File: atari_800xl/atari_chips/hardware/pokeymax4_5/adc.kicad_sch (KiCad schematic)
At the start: 5 parts

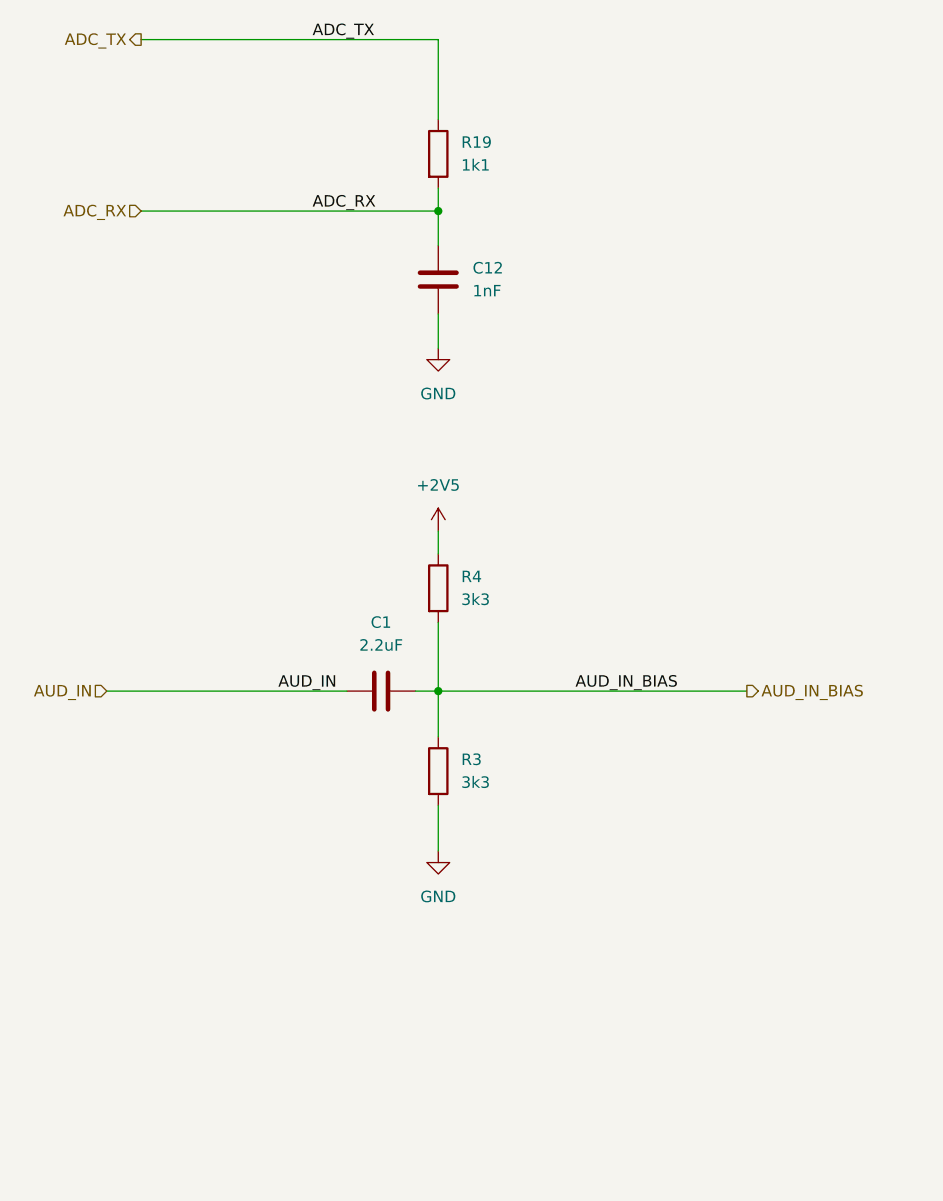
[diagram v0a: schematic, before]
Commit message: After testing 4b first run, there are a few issues. Updated to 4b2 with: Corrected L/R output. ADC bias improvement. ADC preamp out/in- corrected. Moved silkscreen name!
git-svn-id: svn+ssh://192.168.0.3/home/svnfpga/repo/trunk@1476 d6161ac3-aae1-4d52-9b05-ea9ac36b53d3
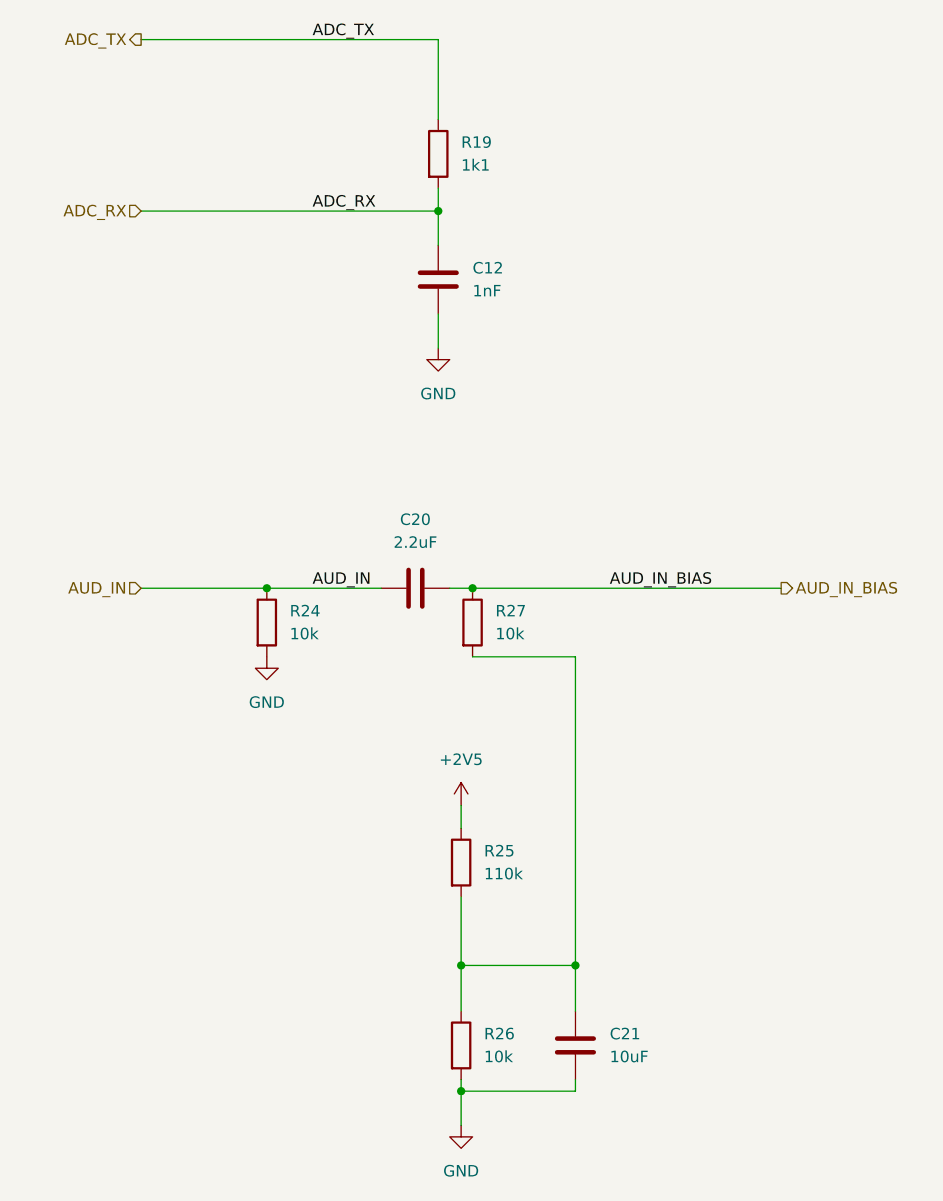
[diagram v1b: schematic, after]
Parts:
- removed C1: 2.2uF, Capacitor_SMD:C_0603_1608Metric, symbol Device:C
- removed R3, R4: 3k3, Resistor_SMD:R_0603_1608Metric, symbol Device:R
- added C20: 2.2uF, Capacitor_SMD:C_0603_1608Metric, symbol Device:C
- added C21: 10uF, Capacitor_SMD:C_0603_1608Metric, symbol Device:C
- added R24, R26, R27: 10k, Resistor_SMD:R_0603_1608Metric, symbol Device:R
- added R25: 110k, Resistor_SMD:R_0603_1608Metric, symbol Device:R
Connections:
- net +2V5: now also R25.1
- net AUD_IN: now also C20.1, R24.1
- net AUD_IN_BIAS: now also C20.2, R27.1
- net GND: now also C21.1, R24.2, R26.2
- new net: C21.2, R25.2, R26.1, R27.2

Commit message: Pokeymax v4_53 as produced
git-svn-id: svn+ssh://192.168.0.3/home/svnfpga/repo/trunk@1512 d6161ac3-aae1-4d52-9b05-ea9ac36b53d3
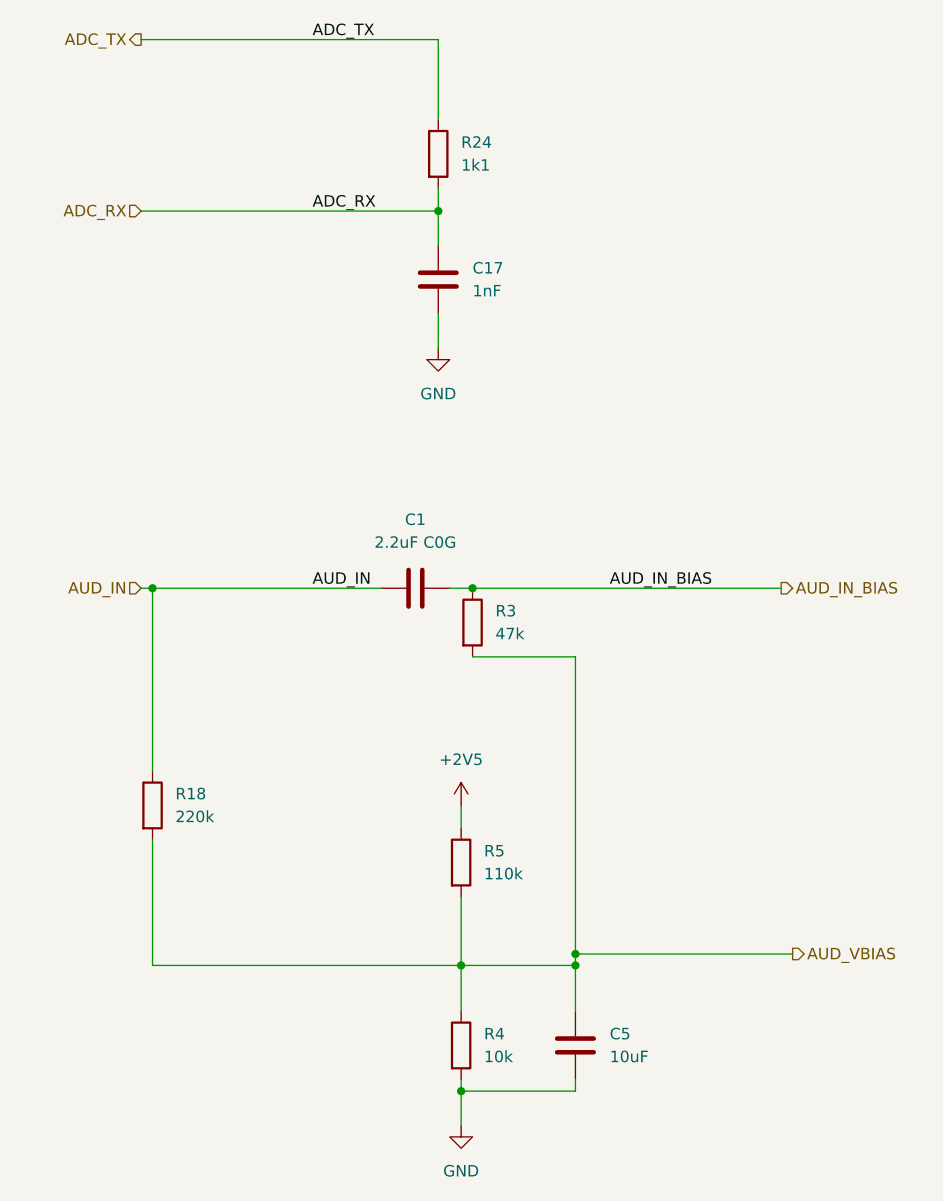
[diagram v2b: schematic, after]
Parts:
- removed R24: 10k, Resistor_SMD:R_0603_1608Metric, symbol Device:R
- added R18: 220k, Resistor_SMD:R_0603_1608Metric, symbol Device:R
- C1: renamed from C20; value 2.2uF -> 2.2uF C0G
- C17: renamed from C12; footprint Capacitor_SMD:C_0603_1608Metric -> Capacitor_SMD:C_0402_1005Metric
- R24: renamed from R19; footprint Resistor_SMD:R_0603_1608Metric -> Resistor_SMD:R_0402_1005Metric
- R3: renamed from R27; value 10k -> 47k
- renumbered C21 to C5, R26 to R4, R25 to R5
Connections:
- net AUD_IN: now also R18.1
- net AUD_VBIAS: now reaches C5.2, R3.2, R4.1, R5.2
- net AUD_VBIAS: now also R18.2
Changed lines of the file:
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@@
 	(paper "A4")
+	(junction
+		(at 80.01 133.35)
+		(diameter 0)
+		(color 0 0 0 0)
+	)
+	(junction
+		(at 33.02 92.71)
+		(diameter 0)
+		(color 0 0 0 0)
+	)
 	(junction
 		(at 80.01 134.62)
@@
 	)
 	(junction
-		(at 45.72 92.71)
-		(diameter 0)
-		(color 0 0 0 0)
-	)
-	(junction
 		(at 68.58 92.71)
 		(diameter 0)
@@
 	(wire
 		(pts
+			(xy 33.02 120.65) (xy 33.02 134.62)
+		)
+		(stroke
+			(width 0)
+			(type default)
+		)
+	)
+	(wire
+		(pts
 			(xy 80.01 100.33) (xy 68.58 100.33)
 		)
@@
 	(wire
 		(pts
-			(xy 80.01 100.33) (xy 80.01 134.62)
+			(xy 80.01 133.35) (xy 104.14 133.35)
+		)
+		(stroke
+			(width 0)
+			(type default)
+		)
+	)
+	(wire
+		(pts
+			(xy 80.01 100.33) (xy 80.01 133.35)
 		)
 		(stroke
@@
 	(wire
 		(pts
-			(xy 31.75 92.71) (xy 45.72 92.71)
+			(xy 31.75 92.71) (xy 33.02 92.71)
 		)
 		(stroke
@@
 	(wire
 		(pts
+			(xy 33.02 92.71) (xy 33.02 113.03)
+		)
+		(stroke
+			(width 0)
+			(type default)
+		)
+	)
+	(wire
+		(pts
 			(xy 64.77 62.23) (xy 64.77 66.04)
 		)
@@
 	(wire
 		(pts
+			(xy 80.01 133.35) (xy 80.01 134.62)
+		)
+		(stroke
+			(width 0)
+			(type default)
+		)
+	)
+	(wire
+		(pts
 			(xy 80.01 139.7) (xy 80.01 134.62)
 		)
@@
 	(wire
 		(pts
-			(xy 45.72 92.71) (xy 58.42 92.71)
+			(xy 33.02 134.62) (xy 67.31 134.62)
+		)
+		(stroke
+			(width 0)
+			(type default)
+		)
+	)
+	(wire
+		(pts
+			(xy 33.02 92.71) (xy 58.42 92.71)
 		)
 		(stroke
@@
 		)
 	)
+	(hierarchical_label "AUD_VBIAS"
+		(shape output)
+		(at 104.14 133.35 0)
+		(effects
+			(font
+				(size 1.27 1.27)
+			)
+			(justify left)
+		)
+	)
 	(hierarchical_label "ADC_TX"
 		(shape output)
@@
 			)
 			(justify right)
+		)
+	)
+	(symbol
+		(lib_id "Device:R")
+		(at 33.02 116.84 0)
+		(unit 1)
+		(exclude_from_sim no)
+		(in_bom yes)
+		(on_board yes)
+		(dnp no)
+		(fields_autoplaced yes)
+		(property "Reference" "R18"
+			(at 35.56 115.5699 0)
+			(effects
+				(font
+					(size 1.27 1.27)
+				)
+				(justify left)
+			)
+		)
+		(property "Value" "220k"
+			(at 35.56 118.1099 0)
+			(effects
+				(font
+					(size 1.27 1.27)
+				)
+				(justify left)
+			)
+		)
+		(property "Footprint" "Resistor_SMD:R_0603_1608Metric"
+			(at 31.242 116.84 90)
+			(effects
+				(font
+					(size 1.27 1.27)
+				)
+				(hide yes)
+			)
+		)
+		(property "Datasheet" "~"
+			(at 33.02 116.84 0)
+			(effects
+				(font
+					(size 1.27 1.27)
+				)
+				(hide yes)
+			)
+		)
+		(property "Description" "Resistor"
+			(at 33.02 116.84 0)
+			(effects
+				(font
+					(size 1.27 1.27)
+				)
+				(hide yes)
+			)
+		)
+		(pin "1"
+		)
+		(pin "2"
+		)
+		(instances
+			(project "pokeymax4_5"
+				(path "/f8f92944-710a-49a0-a698-f840e5f20e15/1dc50d40-2acd-4c26-808b-1819716fc764"
+					(reference "R18")
+					(unit 1)
+				)
+			)
 		)
 	)
@@
 		(dnp no)
 		(fields_autoplaced yes)
-		(property "Reference" "R25"
+		(property "Reference" "R5"
 			(at 69.85 121.9199 0)
 			(effects
@@
 			(project "pokeymax4_5"
 				(path "/f8f92944-710a-49a0-a698-f840e5f20e15/1dc50d40-2acd-4c26-808b-1819716fc764"
-					(reference "R25")
-					(unit 1)
-				)
-			)
-		)
-	)
-	(symbol
-		(lib_id "Device:R")
-		(at 45.72 96.52 0)
-		(unit 1)
-		(exclude_from_sim no)
-		(in_bom yes)
-		(on_board yes)
-		(dnp no)
-		(fields_autoplaced yes)
-		(property "Reference" "R24"
-			(at 48.26 95.2499 0)
-			(effects
-				(font
-					(size 1.27 1.27)
-				)
-				(justify left)
-			)
-		)
-		(property "Value" "10k"
-			(at 48.26 97.7899 0)
-			(effects
-				(font
-					(size 1.27 1.27)
-				)
-				(justify left)
-			)
-		)
-		(property "Footprint" "Resistor_SMD:R_0603_1608Metric"
-			(at 43.942 96.52 90)
-			(effects
-				(font
-					(size 1.27 1.27)
-				)
-				(hide yes)
-			)
-		)
-		(property "Datasheet" "~"
-			(at 45.72 96.52 0)
-			(effects
-				(font
-					(size 1.27 1.27)
-				)
-				(hide yes)
-			)
-		)
-		(property "Description" "Resistor"
-			(at 45.72 96.52 0)
-			(effects
-				(font
-					(size 1.27 1.27)
-				)
-				(hide yes)
-			)
-		)
-		(pin "1"
-		)
-		(pin "2"
-		)
-		(instances
-			(project "pokeymax4_5"
-				(path "/f8f92944-710a-49a0-a698-f840e5f20e15/1dc50d40-2acd-4c26-808b-1819716fc764"
-					(reference "R24")
+					(reference "R5")
 					(unit 1)
 				)
@@
 		(dnp no)
 		(fields_autoplaced yes)
-		(property "Reference" "R27"
+		(property "Reference" "R3"
 			(at 71.12 95.2499 0)
 			(effects
@@
 			)
 		)
-		(property "Value" "10k"
+		(property "Value" "47k"
 			(at 71.12 97.7899 0)
 			(effects
@@
 			(project "pokeymax4_5"
 				(path "/f8f92944-710a-49a0-a698-f840e5f20e15/1dc50d40-2acd-4c26-808b-1819716fc764"
-					(reference "R27")
+					(reference "R3")
 					(unit 1)
 				)
@@
 		(dnp no)
 		(fields_autoplaced yes)
-		(property "Reference" "C20"
+		(property "Reference" "C1"
 			(at 62.23 85.09 90)
 			(effects
@@
 			)
 		)
-		(property "Value" "2.2uF"
+		(property "Value" "2.2uF C0G"
 			(at 62.23 87.63 90)
 			(effects
@@
 			(project "pokeymax4_5"
 				(path "/f8f92944-710a-49a0-a698-f840e5f20e15/1dc50d40-2acd-4c26-808b-1819716fc764"
-					(reference "C20")
+					(reference "C1")
 					(unit 1)
 				)
@@
 		(dnp no)
 		(fields_autoplaced yes)
-		(property "Reference" "R19"
+		(property "Reference" "R24"
 			(at 67.31 43.1799 0)
 			(effects
@@
 			)
 		)
-		(property "Footprint" "Resistor_SMD:R_0603_1608Metric"
+		(property "Footprint" "Resistor_SMD:R_0402_1005Metric"
 			(at 62.992 44.45 90)
 			(effects
@@
 			(project ""
 				(path "/f8f92944-710a-49a0-a698-f840e5f20e15/1dc50d40-2acd-4c26-808b-1819716fc764"
-					(reference "R19")
+					(reference "R24")
 					(unit 1)
 				)
@@
 		(dnp no)
 		(fields_autoplaced yes)
-		(property "Reference" "C12"
+		(property "Reference" "C17"
 			(at 68.58 57.1499 0)
 			(effects
@@
 			)
 		)
-		(property "Footprint" "Capacitor_SMD:C_0603_1608Metric"
+		(property "Footprint" "Capacitor_SMD:C_0402_1005Metric"
 			(at 65.7352 62.23 0)
 			(effects
@@
 			(project ""
 				(path "/f8f92944-710a-49a0-a698-f840e5f20e15/1dc50d40-2acd-4c26-808b-1819716fc764"
-					(reference "C12")
+					(reference "C17")
 					(unit 1)
 				)
@@
 		(dnp no)
 		(fields_autoplaced yes)
-		(property "Reference" "C21"
+		(property "Reference" "C5"
 			(at 83.82 142.2399 0)
 			(effects
@@
 			(project "pokeymax4_5"
 				(path "/f8f92944-710a-49a0-a698-f840e5f20e15/1dc50d40-2acd-4c26-808b-1819716fc764"
-					(reference "C21")
+					(reference "C5")
 					(unit 1)
 				)
@@
 		(dnp no)
 		(fields_autoplaced yes)
-		(property "Reference" "R26"
+		(property "Reference" "R4"
 			(at 69.85 142.2399 0)
 			(effects
@@
 			(project "pokeymax4_5"
 				(path "/f8f92944-710a-49a0-a698-f840e5f20e15/1dc50d40-2acd-4c26-808b-1819716fc764"
-					(reference "R26")
+					(reference "R4")
 					(unit 1)
 				)
@@
 					(unit 1)
 				)
-			)
-		)
-	)
-	(symbol
-		(lib_id "power:GND")
-		(at 45.72 100.33 0)
-		(unit 1)
-		(exclude_from_sim no)
-		(in_bom yes)
-		(on_board yes)
-		(dnp no)
-		(fields_autoplaced yes)
-		(property "Reference" "#PWR041"
-			(at 45.72 106.68 0)
-			(effects
-				(font
-					(size 1.27 1.27)
-				)
-				(hide yes)
-			)
-		)
-		(property "Value" "GND"
-			(at 45.72 105.41 0)
-			(effects
-				(font
-					(size 1.27 1.27)
-				)
-			)
-		)
-		(property "Footprint" ""
-			(at 45.72 100.33 0)
-			(effects
-				(font
-					(size 1.27 1.27)
-				)
-				(hide yes)
-			)
-		)
-		(property "Datasheet" ""
-			(at 45.72 100.33 0)
-			(effects
-				(font
-					(size 1.27 1.27)
-				)
-				(hide yes)
-			)
-		)
-		(property "Description" "Power symbol creates a global label with name \"GND\" , ground"
-			(at 45.72 100.33 0)
-			(effects
-				(font
-					(size 1.27 1.27)
-				)
-				(hide yes)
-			)
-		)
-		(pin "1"
-		)
-		(instances
-			(project "pokeymax4_5"
-				(path "/f8f92944-710a-49a0-a698-f840e5f20e15/1dc50d40-2acd-4c26-808b-1819716fc764"
-					(reference "#PWR041")
-					(unit 1)
-				)
